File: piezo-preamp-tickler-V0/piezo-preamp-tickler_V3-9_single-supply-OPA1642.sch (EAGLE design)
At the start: 49 parts, among them IC1 BQ297X, IC2 SC4503, IC3 TPS7A49, IC4 OPA2134UA, J2 Battery, J3 TRS-1/8"-3.5MM, SW1 SPDT, U2 QS6K1, U3 MCP73831

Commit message: piezo preamp changed back to OPA1642
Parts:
- removed JP1: ICS40300, SparkFun-Connectors:M05LOCK
- removed POT1: 20K, CMU-ArtFab:POT-DUAL-PTV112-4420
- removed U2: QS6K1, CMU-ArtFab:QS6K1
- removed U3: MCP73831, CMU-ArtFab:MCP73831
- added CN1: (no value), adafruit:JST_2PIN-THM
- added D2: B130-13-F, SparkFun:DIODESMA
- added IC5: SC4503, CMU-ArtFab:SC4503
- added IC6: TPS7A49, CMU-ArtFab:TPS7A49
- added J4: (no value), CMU-ArtFab:USB_MICRO-BREDUCED_PASTE
- added J5: Battery, SparkFun-Connectors:CONN_02LOCK
- added Q1: MMBFJ201, CMU-ArtFab:J201SOT-23
- added R17: 2.2k, CMU-ArtFab:R-US_R0603
- added R18: 330, CMU-ArtFab:R-US_R0603
- added R19: 15k, CMU-ArtFab:R-US_R0603
- added R20: 1M, CMU-ArtFab:R-US_R0603
- added R21, R22: 100k, CMU-ArtFab:R-US_R0603
- added R23: 11k, CMU-ArtFab:R-US_R0603
- added SW2: INPUT-select, CMU-ArtFab:SWITCH_SPDTCL-SB-12B
- added SW3: SPDT, CMU-ArtFab:SWITCH_SPDTCL-SB-12B
- C1: value 4.7uF -> 10uF; device rcl:C-EUC0603 -> adafruit:C-USC0805K
- C10: value 10nF -> 2.2pF
- C11: value 10uF -> 68uF; device rcl:C-EUC0603 -> rcl:C-EUC1206
- C12: device rcl:C-EUC1206 -> rcl:C-EUC0603
- C13: value 0.1uF -> 10nF; device adafruit:C-USC0805 -> rcl:C-EUC0603
- C14: value 10uF -> 10nF; device adafruit:C-USC0805 -> rcl:C-EUC0603
- C15: value 0.1uF -> 10uF; device adafruit:C-USC0805K -> rcl:C-EUC0603
- C16: value 10uF -> 4.7uF; device adafruit:C-USC0805 -> rcl:C-EUC0603
- C2: value 4.7uF -> 100uF; device rcl:C-EUC0603 -> resistor:CPOL-EUC
- C3: device rcl:C-EUC0603 -> adafruit:C-USC0805K
- C4: value 10uF -> 0.1uF; device rcl:C-EUC0603 -> adafruit:C-USC0805K
- C5: value 56nF -> 10uF; device rcl:C-EUC0603 -> resistor:CPOL-EUB
- C6: value 2.2pF -> 4.7uF
- C7: value 68uF -> 0.1uF; device rcl:C-EUC1206 -> rcl:C-EUC0603
- C9: value 10nF -> 56nF
- D1: value B130-13-F -> BAT54S; device SparkFun:DIODESMA -> diode:BAT54S
- IC1: value BQ297X -> OPA1642; device CMU-ArtFab:BQ297X-BATTERY-MANAGERLONG -> linear:TL072D
- IC2: value SC4503 -> MCP73831; device CMU-ArtFab:SC4503 -> CMU-ArtFab:MCP73831
- IC3: value TPS7A49 -> QS6K1; device CMU-ArtFab:TPS7A49 -> CMU-ArtFab:QS6K1
- IC4: value OPA2134UA -> BQ297X; device linear:OPA2134UA -> CMU-ArtFab:BQ297X-BATTERY-MANAGERLONG
- J1: value (none) -> HEADPHONES; device CMU-ArtFab:USB_MICRO-BREDUCED_PASTE -> CMU-ArtFab:TRRS-1/8"-3.5MMLGPADS
- J2: value Battery -> PHONE; device SparkFun-Connectors:CONN_02LOCK -> CMU-ArtFab:TRRS-1/8"-3.5MMLGPADS
- J3: value TRS-1/8"-3.5MM -> Mixer
- L1: value 2.7uH -> 100uH/±5%/500mA; device SparkFun-Passives:INDUCTORCR54 -> rcl:L-EUL3225M
- L2: value 100uH/500mA -> 2.7uH; device rcl:L-EUL3225M -> SparkFun-Passives:INDUCTORCR54
- LED1: value (none) -> Power
- R1: value 390 -> 100K
- R10: value 100k -> 1.2K
- R11: value 100k -> 2.2K
- R12: value 11k -> 390
- R13: value 150k -> 5k
- R14: value 150k -> 470
- R15, R16: value 1k -> 10M
- R2: value 5k -> 10M
- R3, R4: value 10M -> 100K
- R5: value 470 -> 2.2K
- R6: value 2.2k -> 50K; device CMU-ArtFab:R-US_R0603 -> CMU-ArtFab:POTTHUMBPOT14
- R7: value 330 -> 220
- R8: value 15k -> 1K
- SW1: value SPDT -> SWITCH_DPDT; device CMU-ArtFab:SWITCH_SPDTCL-SB-12B -> CMU-ArtFab:SWITCH_DPDT
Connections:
- removed net N$15: C15.1, IC4A.V+, L2.2, R13.2
- removed net N$47: C9.2, IC3.FB, R11.2, R12.1
- removed net N$48: C10.1, IC3.NR/SS
- new net N$1: D1.C2, IC1A.+IN, R1.2, R2.2
- new net N$16: C5.-, SW1.P$5
- new net N$17: J2.SLEEVE, SW2.2
- new net N$18: LED1.A, R12.1
- new net N$19: SW1.P$1, SW2.1
- new net N$24: C2.+, IC1A.-IN, IC1A.OUT
- new net N$26: C13.2, IC6.FB, R22.2, R23.1
- new net N$28: C14.1, IC6.NR/SS
- new net N$29: C9.1, IC5.SHDN, R19.1
- new net N$30: C10.2, IC5.FB, R20.1, R21.2
- new net N$32: D2.A, IC5.SW, L2.2
- new net N$33: J1.TIP, J2.TIP
- new net SELECT: Q1.D, R11.2, SW1.P$2
- net +12V: now also C12.1, C13.1, IC6.OUT, L1.1, R22.1; no longer C8.1, C9.1, IC3.OUT, JP1.1, L2.1, R11.1
- net +5V: now also C6.1, IC2.4VDD, J4.VBUS; no longer C1.1, J1.VBUS, U3.4VDD
- net BATGND: now also C7.1, IC3.6D1, IC4.VSS, SW3.2; no longer C3.1, IC1.VSS, SW1.2, U2.6D1
- net GND: now also C1.2, C12.2, C14.2, C3.2, C9.2, CN1.2, D1.A1, IC1P.V-, IC3.2S2, IC5.GND, IC6.GND, J1.RING2, J2.RING2, R11.1, R15.1, R16.1, R17.1, R21.1, R23.2, R9.1; no longer C10.2, C13.2, C5.2, C7.2, IC2.GND, IC3.GND, IC4A.V-, JP1.3, R12.2, R14.1, R3.1, R6.1, U2.2S2
- net N$10: now also Q1.G, R8.1, R9.2; no longer C16.1, IC4B.OUT, POT1/2.S
- net N$11: now also R8.2, SW1.P$4; no longer U2.4D2, U2.5S1
- net N$12: now also J3.RING1, J3.TIP, SW1.P$6; no longer D1.A, IC2.SW, L1.2
- net N$13: now also J1.RING1, J2.RING1; no longer C5.1, IC2.SHDN, R8.1
- net N$14: now also C2.-, R5.1; no longer C6.2, IC2.FB, R10.2, R9.1
- net N$2: now also CN1.1; no longer LED1.A
- net N$21: now also IC2.5PROG, R13.2; no longer IC4B.-IN, POT1/2.E, R16.2
- net N$22: now also R14.1; no longer R5.1
- net N$23: now also IC3.4D2, IC3.5S1; no longer C12.2, R15.1
- net N$25: now also IC2.1STAT, R14.2; no longer R5.2, U3.1STAT
- net N$27: now also IC3.1G1, IC4.DRAIN-FET, R15.2; no longer IC1.DRAIN-FET, R3.2, U2.1G1
- net N$3: now also Q1.S, R10.2; no longer C12.1, JP1.4
- net N$31: now also IC3.3G2, IC4.CHG-FET, R16.2; no longer IC1.CHG-FET, R4.2, U2.3G2
- net N$34: now also IC4.V-, R17.2; no longer IC1.V-, R6.2
- net N$4: now also J1.SLEEVE, SW2.3; no longer C14.2, R16.1
- net N$42: now also C7.2, IC4.BAT, R18.2; no longer C3.2, IC1.BAT, R7.2
- net N$5: now also IC1B.+IN, R7.1; no longer IC4A.-IN, POT1/1.E, R15.2
- net N$6: now also C5.+, IC1B.OUT, R6.WIPER; no longer R2.2, U3.5PROG
- net N$7: now also IC1B.-IN, R5.2, R6.OUT; no longer C16.2, J3.RING1, J3.TIP
- net N$8: now also C4.1, IC1P.V+, L1.2, R3.2; no longer C13.1, IC4A.+IN, IC4B.+IN, R13.1, R14.2
- net N$9: now also C1.1, C3.1, R2.1, R3.1, R4.2, R7.2; no longer C14.1, IC4A.OUT, POT1/1.S
- net USBGND: now also C16.2, C6.2, IC2.2VSS, J4.GND, J5.2, R13.1, SW3.1; no longer C1.2, C2.2, J1.GND, J2.2, R2.1, SW1.1, U3.2VSS
- net V+: now also C10.1, C15.1, D2.C, IC6.EN, IC6.IN, R20.2; no longer C6.1, C7.1, D1.C, IC3.EN, IC3.IN, R9.2
- net VBAT: now also C16.1, C8.1, IC2.3VBAT, IC5.IN, J5.1, L2.1, R12.2, R18.1, R19.2; no longer C2.1, C4.1, IC2.IN, J2.1, L1.1, R1.2, R7.1, R8.2, U3.3VBAT
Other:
- note added: ""A Discrete FET Guitar Preamp" by J. Donald Tillman"
- note added: ""Simple JFET Preamp for an iDevice Guitar Interface""
- note added: "<- PASS PHONE HEADPHONE OUTPUT TO HEADPHONE JACK"
- note added: "Buffer-Stage-1"
- note added: "Buffer-Stage-2"
- note added: "HEADSET IS USED ONLY WITH PHONE"
- note added: "MIXER OUT IS STANDARD 1/8" STEREO TRS"
- note added: "OpAmp-Amplifier"
- note added: "T - Left R1 - Right R2 - Ground S - Mic"
- note added: "This DPDT switch totally isolates Buffer-Stage when in the lower position (i.e. the input to and the output from the buffer stage are no longer connected"

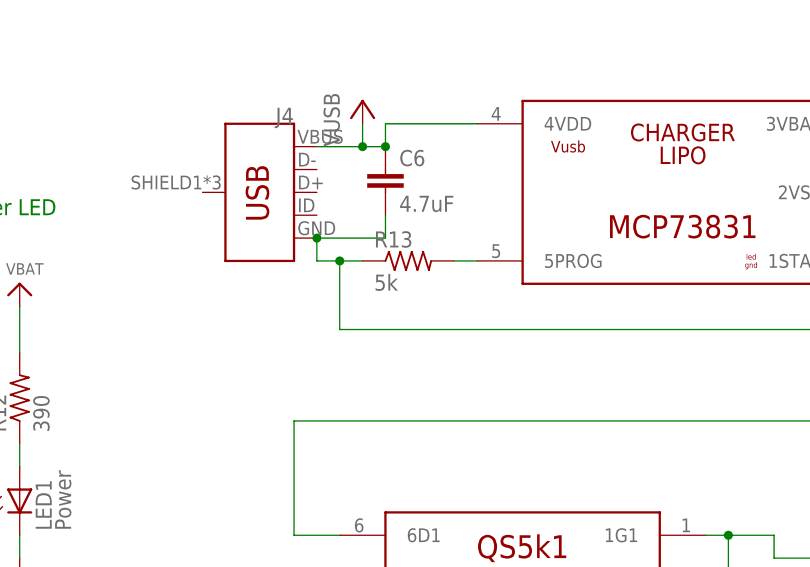
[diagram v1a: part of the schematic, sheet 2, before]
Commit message: resolved cosmetic issues in mems and piezo for 5k and 50k resistor values that should be 4.7k and 47K
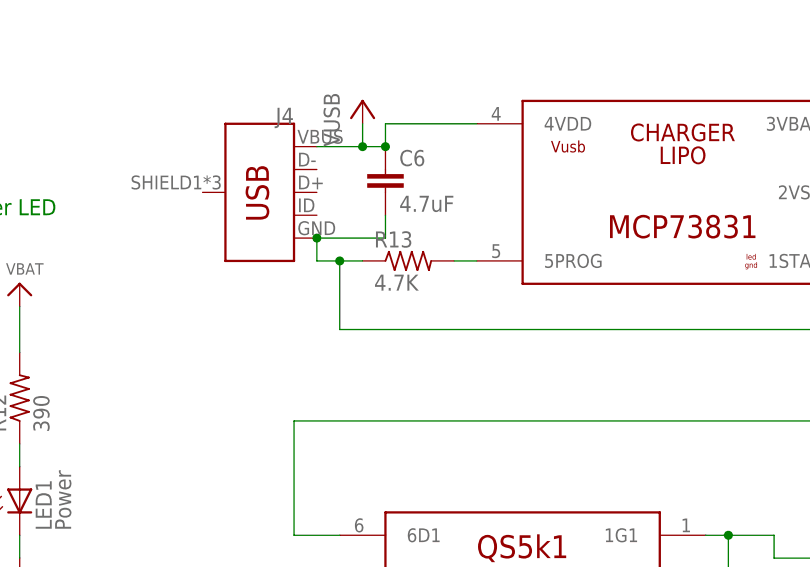
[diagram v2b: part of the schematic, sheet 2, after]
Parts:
- R13: value 5k -> 4.7K
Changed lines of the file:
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@@
 <part name="LED2" library="led" library_urn="urn:adsk.eagle:library:259" deviceset="LED" device="3MM" package3d_urn="urn:adsk.eagle:package:15797/1" value="Charge"/>
 <part name="R14" library="CMU-ArtFab" deviceset="R-US_" device="R0603" value="470"/>
-<part name="R13" library="CMU-ArtFab" deviceset="R-US_" device="R0603" value="5k"/>
+<part name="R13" library="CMU-ArtFab" deviceset="R-US_" device="R0603" value="4.7K"/>
 <part name="IC4" library="CMU-ArtFab" deviceset="BQ297X-BATTERY-MANAGER" device="LONG" value="BQ297X"/>
 <part name="U3" library="microbuilder" deviceset="VBAT" device=""/>

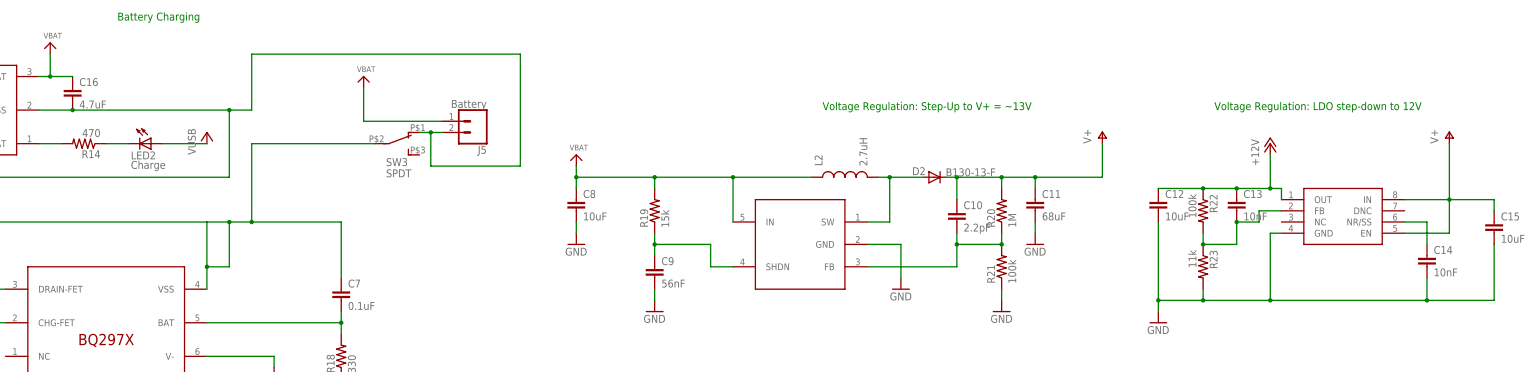
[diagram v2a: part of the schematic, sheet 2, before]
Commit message: capacitors renumbered in sequence
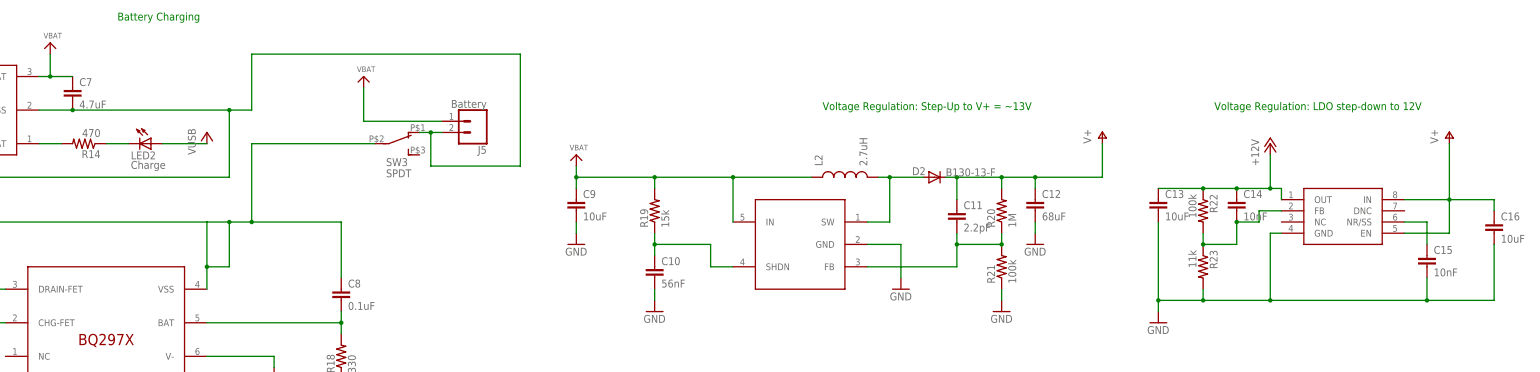
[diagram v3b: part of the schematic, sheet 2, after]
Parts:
- C10: value 2.2pF -> 56nF
- C11: value 68uF -> 2.2pF; device rcl:C-EUC1206 -> rcl:C-EUC0603
- C12: value 10uF -> 68uF; device rcl:C-EUC0603 -> rcl:C-EUC1206
- C13: value 10nF -> 10uF
- C15: value 10uF -> 10nF
- C16: value 4.7uF -> 10uF
- C7: value 0.1uF -> 4.7uF
- C8: value 10uF -> 0.1uF
- C9: value 56nF -> 10uF
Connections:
- net +12V: now also C14.1; no longer C12.1
- net BATGND: now also C8.1; no longer C7.1
- net GND: now also C10.2, C13.2, C16.2; no longer C11.2, C14.2, C8.2
- net N$26: now also C14.2; no longer C13.2
- net N$28: now also C15.1; no longer C14.1
- net N$29: now also C10.1; no longer C9.1
- net N$30: now also C11.2; no longer C10.2
- net N$42: now also C8.2; no longer C7.2
- net USBGND: now also C7.2; no longer C16.2
- net V+: now also C12.1, C16.1; no longer C10.1, C15.1
- net VBAT: now also C7.1, C9.1; no longer C16.1, C8.1
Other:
- moved on the sheet: C10, C11, C12, C13, C14, C15, C16, C7, C8, C9

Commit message: OPA1642 device added from CMU artfab library
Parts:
- IC1: device linear:TL072D -> CMU-ArtFab:OPA1642
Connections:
- net GND: now also IC1G$1.V-; no longer IC1P.V-
- net N$1: now also IC1G$1.+IN; no longer IC1A.+IN
- net N$24: now also IC1G$1.-IN, IC1G$1.OUT; no longer IC1A.-IN, IC1A.OUT
- net N$5: now also IC1G$2.+IN; no longer IC1B.+IN
- net N$6: now also IC1G$2.OUT; no longer IC1B.OUT
- net N$7: now also IC1G$2.-IN; no longer IC1B.-IN
- net N$8: now also IC1G$1.V+; no longer IC1P.V+
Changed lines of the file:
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@@
 <part name="P+2" library="supply1" library_urn="urn:adsk.eagle:library:371" deviceset="+5V" device="" value="VUSB"/>
 <part name="P+3" library="supply1" library_urn="urn:adsk.eagle:library:371" deviceset="+5V" device="" value="VUSB"/>
-<part name="IC1" library="linear" library_urn="urn:adsk.eagle:library:262" deviceset="TL072" device="D" package3d_urn="urn:adsk.eagle:package:16404/2" value="OPA1642"/>
 <part name="C5" library="resistor" library_urn="urn:adsk.eagle:library:348" deviceset="CPOL-EU" device="B" package3d_urn="urn:adsk.eagle:package:25911/1" value="10uF"/>
 <part name="C2" library="resistor" library_urn="urn:adsk.eagle:library:348" deviceset="CPOL-EU" device="C" package3d_urn="urn:adsk.eagle:package:25913/1" value="100uF"/>
+<part name="IC1" library="CMU-ArtFab" deviceset="OPA1642" device="" package3d_urn="urn:adsk.eagle:package:16404/2"/>
 </parts>
 <sheets>
@@
 </instance>
 <instance part="R6" gate="G$1" x="73.66" y="17.78"/>
-<instance part="IC1" gate="A" x="20.32" y="27.94"/>
-<instance part="IC1" gate="B" x="86.36" y="30.48"/>
-<instance part="IC1" gate="P" x="20.32" y="27.94"/>
 <instance part="C5" gate="G$1" x="99.06" y="30.48" rot="R90"/>
 <instance part="C2" gate="G$1" x="43.18" y="27.94" rot="R90"/>
+<instance part="IC1" gate="G$1" x="20.32" y="27.94"/>
+<instance part="IC1" gate="G$2" x="86.36" y="30.48"/>
 </instances>
 <busses>
@@
 <wire x1="20.32" y1="10.16" x2="20.32" y2="20.32" width="0.1524" layer="91"/>
 <pinref part="SUPPLY2" gate="GND" pin="GND"/>
-<pinref part="IC1" gate="P" pin="V-"/>
+<pinref part="IC1" gate="G$1" pin="V-"/>
 </segment>
 <segment>
@@
 <wire x1="73.66" y1="43.18" x2="73.66" y2="33.02" width="0.1524" layer="91"/>
 <wire x1="73.66" y1="33.02" x2="78.74" y2="33.02" width="0.1524" layer="91"/>
-<pinref part="IC1" gate="B" pin="+IN"/>
+<pinref part="IC1" gate="G$2" pin="+IN"/>
 </segment>
 </net>
@@
 <wire x1="96.52" y1="17.78" x2="96.52" y2="30.48" width="0.1524" layer="91"/>
 <pinref part="R6" gate="G$1" pin="WIPER"/>
-<pinref part="IC1" gate="B" pin="OUT"/>
 <pinref part="C5" gate="G$1" pin="+"/>
 <junction x="96.52" y="30.48"/>
+<pinref part="IC1" gate="G$2" pin="OUT"/>
 </segment>
 </net>
@@
 <wire x1="73.66" y1="22.86" x2="73.66" y2="27.94" width="0.1524" layer="91"/>
 <junction x="73.66" y="27.94"/>
-<pinref part="IC1" gate="B" pin="-IN"/>
+<pinref part="IC1" gate="G$2" pin="-IN"/>
 </segment>
 </net>
@@
 <net name="N$24" class="0">
 <segment>
-<wire x1="27.94" y1="27.94" x2="33.02" y2="27.94" width="0.1524" layer="91"/>
+<wire x1="30.48" y1="27.94" x2="33.02" y2="27.94" width="0.1524" layer="91"/>
 <wire x1="33.02" y1="27.94" x2="33.02" y2="12.7" width="0.1524" layer="91"/>
 <wire x1="10.16" y1="12.7" x2="33.02" y2="12.7" width="0.1524" layer="91"/>
-<wire x1="10.16" y1="25.4" x2="12.7" y2="25.4" width="0.1524" layer="91"/>
+<wire x1="10.16" y1="25.4" x2="15.24" y2="25.4" width="0.1524" layer="91"/>
 <wire x1="10.16" y1="12.7" x2="10.16" y2="25.4" width="0.1524" layer="91"/>
 <wire x1="40.64" y1="27.94" x2="33.02" y2="27.94" width="0.1524" layer="91"/>
 <junction x="33.02" y="27.94"/>
-<pinref part="IC1" gate="A" pin="-IN"/>
-<pinref part="IC1" gate="A" pin="OUT"/>
 <pinref part="C2" gate="G$1" pin="+"/>
+<pinref part="IC1" gate="G$1" pin="-IN"/>
+<pinref part="IC1" gate="G$1" pin="OUT"/>
 </segment>
 </net>
@@
 <wire x1="-38.1" y1="43.18" x2="-38.1" y2="55.88" width="0.1524" layer="91"/>
 <wire x1="-25.4" y1="55.88" x2="-38.1" y2="55.88" width="0.1524" layer="91"/>
-<wire x1="12.7" y1="30.48" x2="-25.4" y2="30.48" width="0.1524" layer="91"/>
+<wire x1="15.24" y1="30.48" x2="-25.4" y2="30.48" width="0.1524" layer="91"/>
 <wire x1="-25.4" y1="30.48" x2="-25.4" y2="55.88" width="0.1524" layer="91"/>
 <wire x1="-43.18" y1="55.88" x2="-38.1" y2="55.88" width="0.1524" layer="91"/>
 <junction x="-38.1" y="55.88"/>
-<pinref part="IC1" gate="A" pin="+IN"/>
+<pinref part="IC1" gate="G$1" pin="+IN"/>
 </segment>
 </net>
@@
 <wire x1="81.28" y1="73.66" x2="20.32" y2="73.66" width="0.1524" layer="91"/>
 <wire x1="20.32" y1="73.66" x2="20.32" y2="68.58" width="0.1524" layer="91"/>
-<pinref part="IC1" gate="P" pin="V+"/>
-</segment>
-</net>
+<pinref part="IC1" gate="G$1" pin="V+"/>
+</segment>
+</net>
